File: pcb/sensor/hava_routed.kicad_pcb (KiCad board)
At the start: 2 copper layers, 14 x 16 mm, 6 parts, among them J1 Conn_01x04, U1 BME280

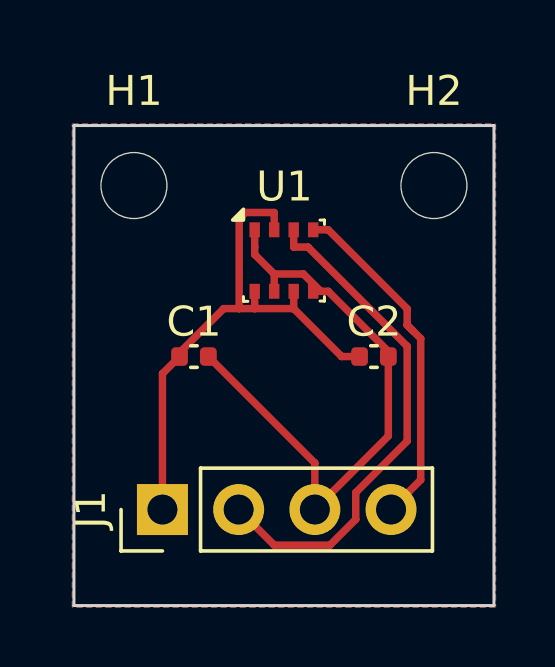
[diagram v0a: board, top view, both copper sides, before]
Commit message: Şematik akışı: kartlar KiCad şematiğinden kuruluyor
Önceden SKiDL netlistinden doğrudan PCB üretiliyordu, arada şematik yoktu.
Artık akış: SKiDL devre tanımı -> KiCad şematiği (hava.kicad_sch) -> ERC ->
şematikten netlist -> PCB yerleşimi -> yol çizimi -> DRC (şematik paritesiyle).

- pcb/tools/sch_gen.py: netlistten KiCad şematiği üretir (İngilizce blok başlıkları)
- pcb/tools/check.sh: şematik üretimi, ERC, netlist karşılaştırması, PDF çıktısı
- pcb/tools/relink_board.py: yolları bozmadan footprint'leri şematiğe yeniden bağlar
- İsimsiz netlere ad verildi: USB_CC1/2, IO2_PU, IO8_PU, LED_A
- Sonuç: ERC 0 hata, DRC 0 ihlal, 0 bağlanmamış pad, şematik-PCB paritesi temiz
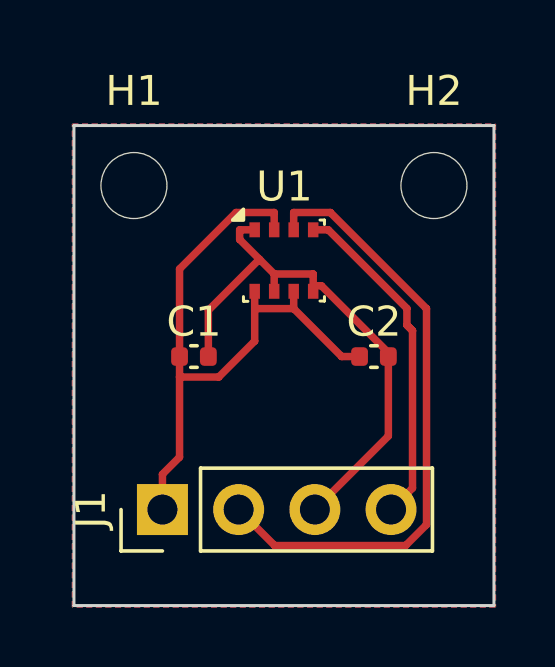
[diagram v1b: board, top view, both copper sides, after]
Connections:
- net I2C_SCL renamed /I2C_SCL
- net I2C_SDA renamed /I2C_SDA
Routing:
- net /I2C_SDA: track 17.0 -> 20.6 mm
- net +3V3: track 18.7 -> 22.2 mm
- net GND: track 20.3 -> 18.5 mm
